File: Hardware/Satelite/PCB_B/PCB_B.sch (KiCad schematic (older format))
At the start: 31 parts, among them IC1 MCP1642B-50I_MS, J1 Conector_PCB_B-C, J2 Conector_PCB_A-B, M1 Spacer, M2 Spacer, M3 Spacer, U1 MIC5323-3.3YD5_TR

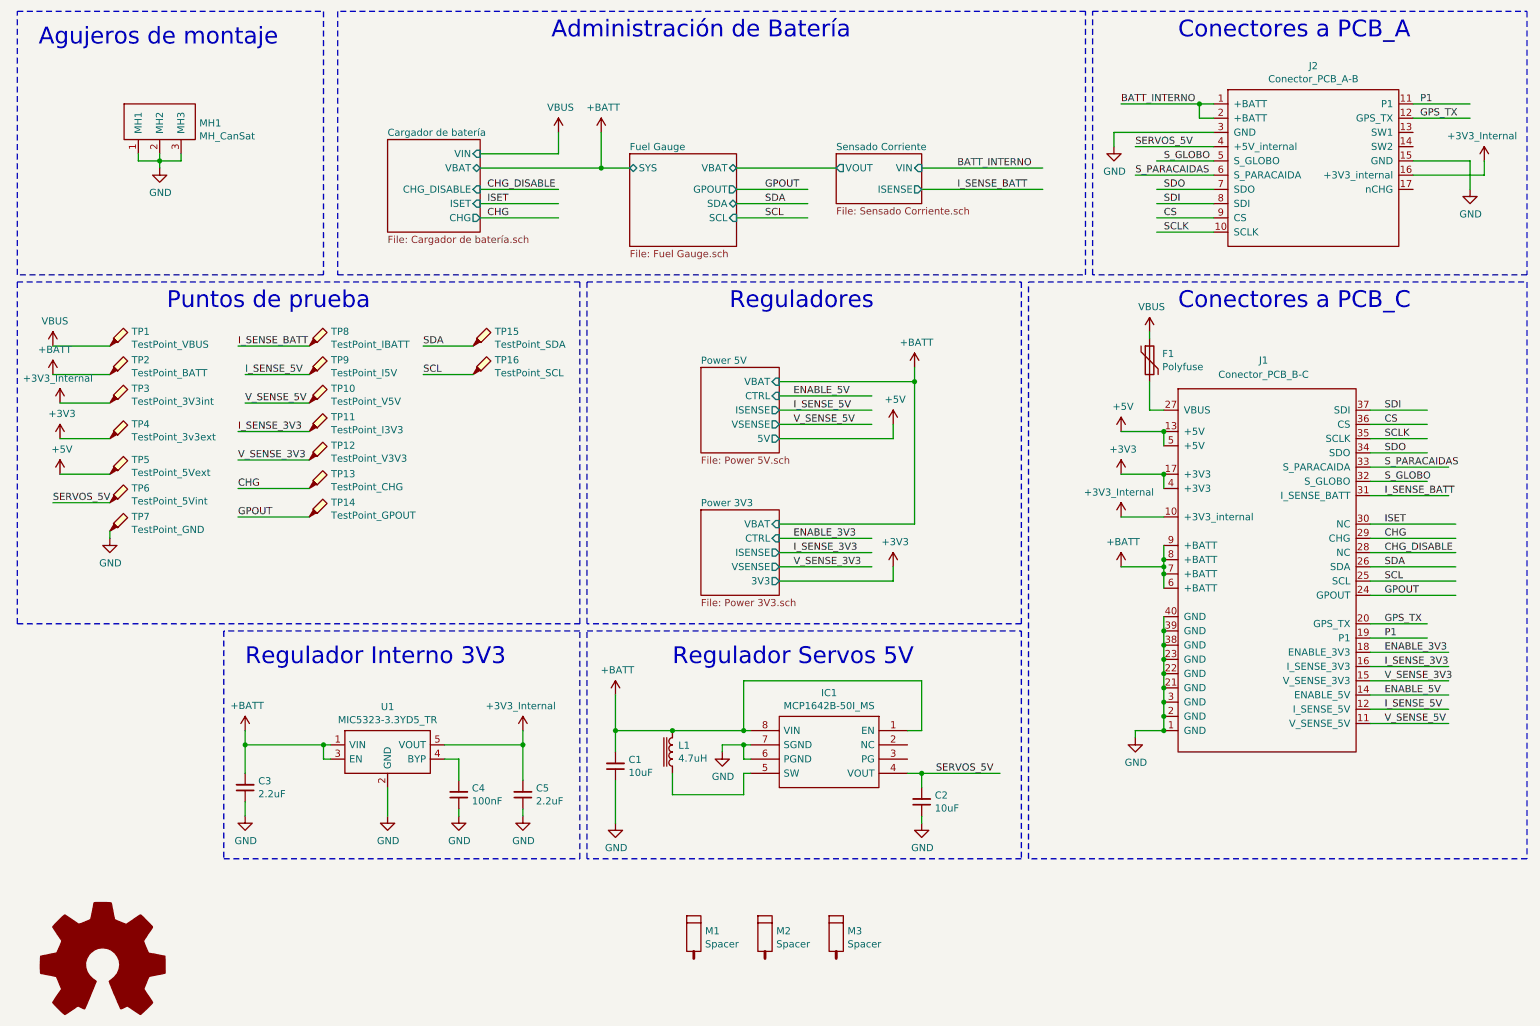
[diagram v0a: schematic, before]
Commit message: Arreglos en PCB_A y PCB_B:
- El CI cargador de batería ya no alimenta al sistema, al conectar un cargador el mismo alimenta a la batería y al sistema de manera simultánea
- Ya no es necesario encender el CanSat para cargar la batería
- El interruptor del PCB_A ahora apaga todo el sistema independientemente si se está cargando o no la batería
- Agregado LED indicador de carga de batería
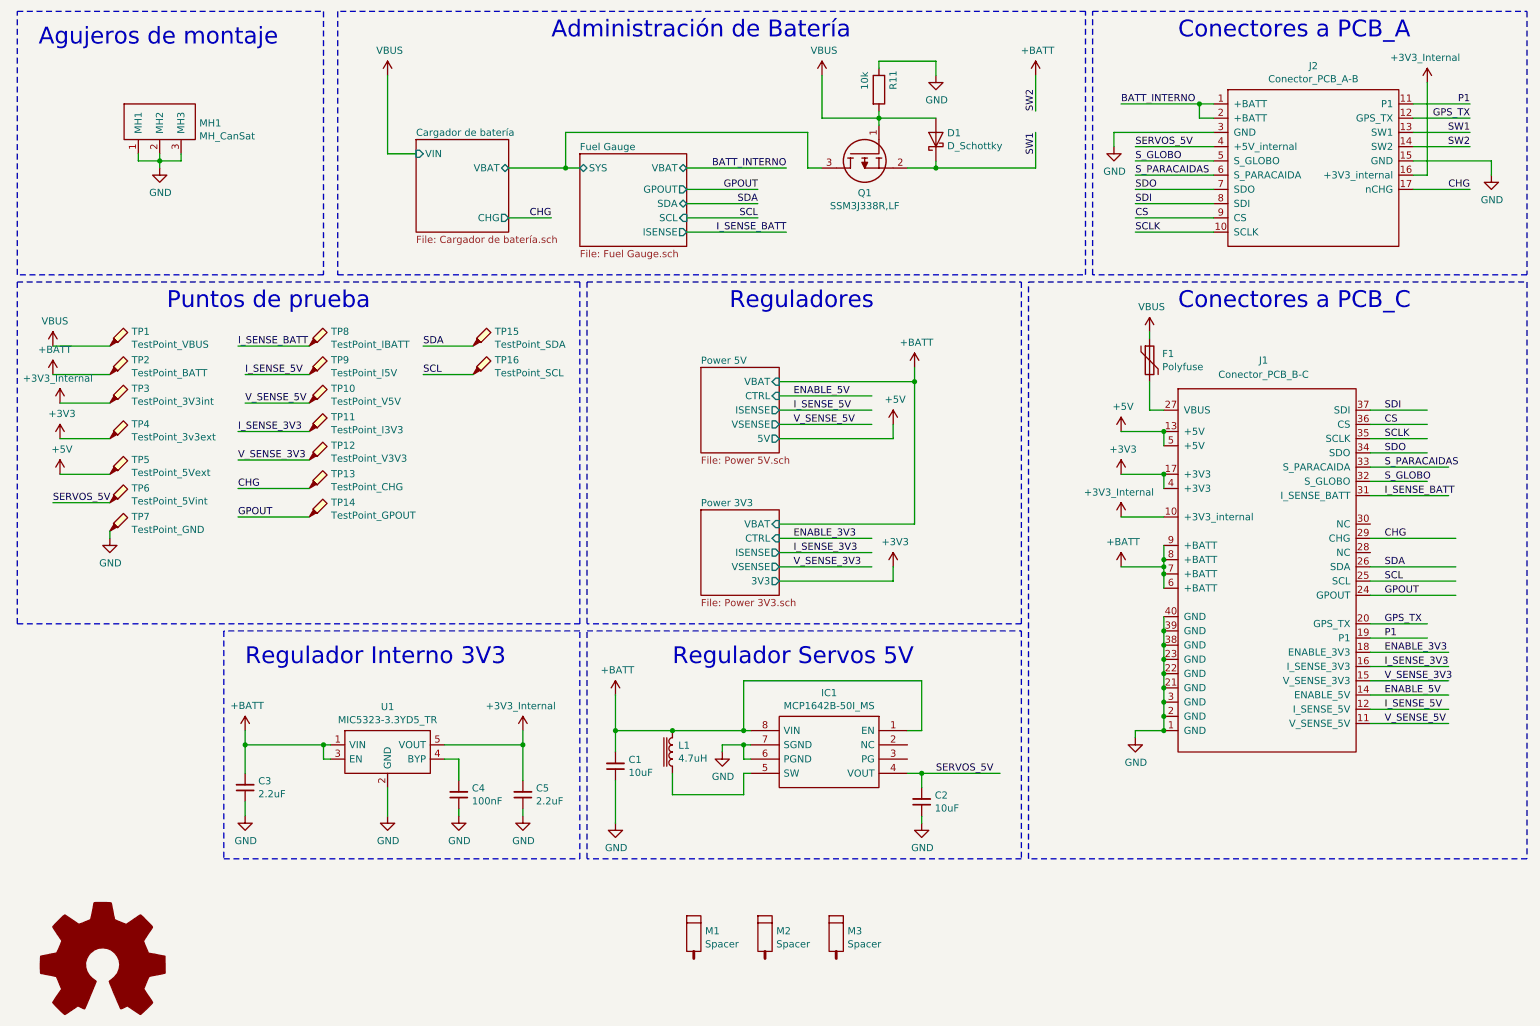
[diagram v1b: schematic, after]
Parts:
- added D1: D_Schottky, Diode_SMD:D_SMB, symbol Device:D_Schottky
- added Q1: SSM3J338R,LF, SamacSys_Parts:SSM3J332RLFT, symbol SamacSys_Parts:SSM3J338R,LF
- added R11: 10k, Capacitor_SMD:C_0603_1608Metric_Pad1.05x0.95mm_HandSolder, symbol Device:R
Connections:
- net labels added: SW1, SW2
- net labels removed: CHG_DISABLE, ISET
- wire segments 151 -> 165

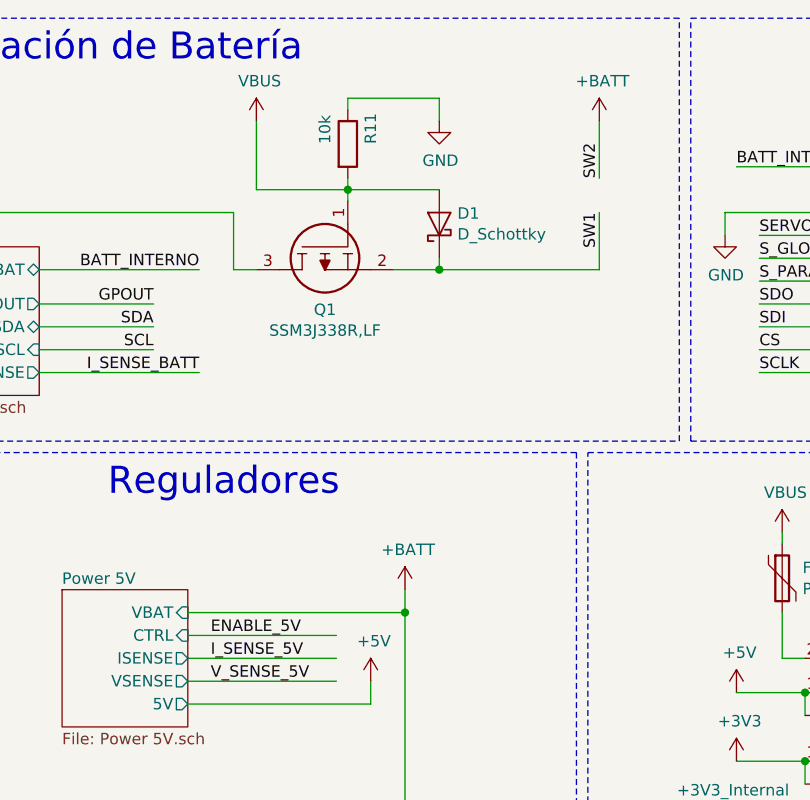
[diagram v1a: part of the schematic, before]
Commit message: Corregido MOSFET Q1 con drenador y surtidor invertidos
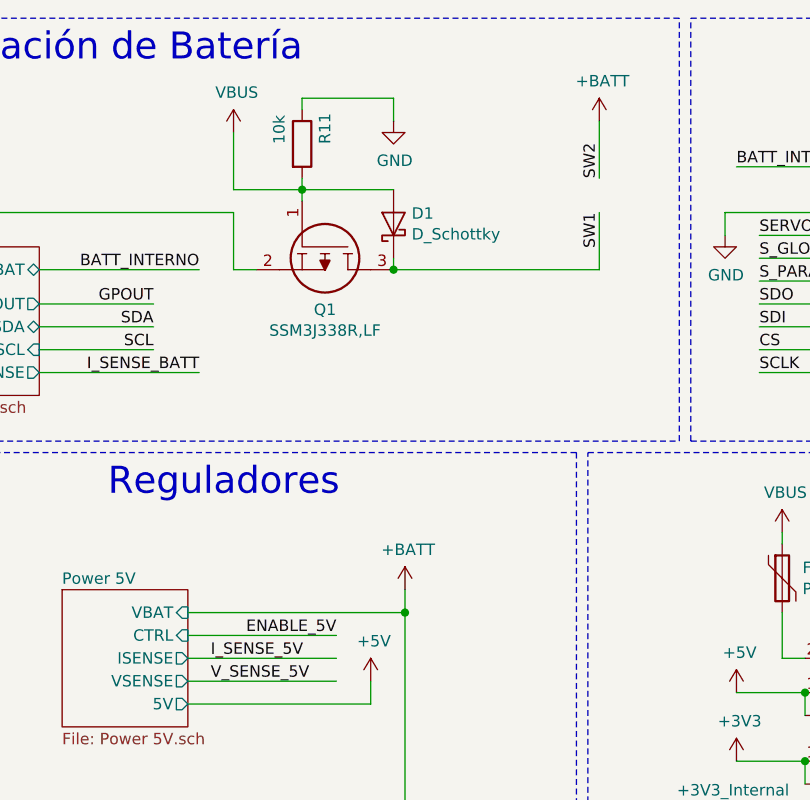
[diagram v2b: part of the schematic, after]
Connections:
- wire segments 165 -> 164
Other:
- moved on the sheet: D1, R11
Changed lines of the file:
@@
 Text Label 6000 4250 0    50   ~ 0
 ENABLE_3V3
-Text Label 6000 3250 0    50   ~ 0
+Text Label 6550 3250 2    50   ~ 0
 ENABLE_5V
 Wire Wire Line
@@
 Text Label 5950 1650 2    50   ~ 0
 BATT_INTERNO
-Connection ~ 7000 1650
-Wire Wire Line
-	7000 1650 7700 1650
-Wire Wire Line
-	6800 1650 7000 1650
-Wire Wire Line
-	7000 1600 7000 1650
 $Comp
 L Device:D_Schottky D1
 U 1 1 5CD2E872
-P 7000 1450
-F 0 "D1" V 7046 1371 50  0000 R CNN
-F 1 "D_Schottky" V 6955 1371 50  0000 R CNN
-F 2 "Diode_SMD:D_SMB" H 7000 1450 50  0001 C CNN
-F 3 "~" H 7000 1450 50  0001 C CNN
-F 4 "MBRS2040LT3G" V 7000 1450 50  0001 C CNN "Manufacturer Part Number"
-	1    7000 1450
+P 6800 1450
+F 0 "D1" V 6846 1371 50  0000 R CNN
+F 1 "D_Schottky" V 6755 1371 50  0000 R CNN
+F 2 "Diode_SMD:D_SMB" H 6800 1450 50  0001 C CNN
+F 3 "~" H 6800 1450 50  0001 C CNN
+F 4 "MBRS2040LT3G" V 6800 1450 50  0001 C CNN "Manufacturer Part Number"
+	1    6800 1450
 	0    -1   -1   0
 $EndComp
 Wire Wire Line
-	6600 1250 6600 1300
-Wire Wire Line
-	7000 900  7000 1000
-Wire Wire Line
-	6600 950  6600 900
-Connection ~ 6600 1300
-Wire Wire Line
-	6600 1350 6600 1300
-Wire Wire Line
-	7000 1300 6600 1300
+	6400 1250 6400 1300
+Wire Wire Line
+	6800 900  6800 1000
+Wire Wire Line
+	6400 950  6400 900
+Connection ~ 6400 1300
+Wire Wire Line
+	6400 1350 6400 1300
+Wire Wire Line
+	6800 1300 6400 1300
 $Comp
 L power:GND #PWR?
 U 1 1 5CCDA8EC
-P 7000 1000
+P 6800 1000
 AR Path="/5BB6C3A1/5CCDA8EC" Ref="#PWR?"  Part="1"
 AR Path="/5BB6C83B/5CCDA8EC" Ref="#PWR?"  Part="1"
 AR Path="/5BC14C3C/5CCDA8EC" Ref="#PWR?"  Part="1"
 AR Path="/5CCDA8EC" Ref="#PWR017"  Part="1"
-F 0 "#PWR017" H 7000 750 50  0001 C CNN
-F 1 "GND" H 7005 827 50  0000 C CNN
-F 2 "" H 7000 1000 50  0001 C CNN
-F 3 "" H 7000 1000 50  0001 C CNN
-	1    7000 1000
+F 0 "#PWR017" H 6800 750 50  0001 C CNN
+F 1 "GND" H 6805 827 50  0000 C CNN
+F 2 "" H 6800 1000 50  0001 C CNN
+F 3 "" H 6800 1000 50  0001 C CNN
+	1    6800 1000
 	1    0    0    -1
 $EndComp
@@
 L Device:R R?
 U 1 1 5CCCB39F
-P 6600 1100
+P 6400 1100
 AR Path="/5BA17F9C/5CCCB39F" Ref="R?"  Part="1"
 AR Path="/5BA1A7F9/5CCCB39F" Ref="R?"  Part="1"
@@
 AR Path="/5BB1631B/5CCCB39F" Ref="R?"  Part="1"
 AR Path="/5BC28DAC/5CCCB39F" Ref="R?"  Part="1"
-F 0 "R11" V 6700 1100 50  0000 L CNN
-F 1 "10k" V 6500 1100 50  0000 L CNN
-F 2 "Capacitor_SMD:C_0603_1608Metric_Pad1.05x0.95mm_HandSolder" V 6530 1100 50  0001 C CNN
-F 3 "~" H 6600 1100 50  0001 C CNN
-F 4 "RC0603JR-0710KL" V 6600 1100 50  0001 C CNN "Manufacturer Part Number"
-	1    6600 1100
+F 0 "R11" V 6500 1100 50  0000 L CNN
+F 1 "10k" V 6300 1100 50  0000 L CNN
+F 2 "Capacitor_SMD:C_0603_1608Metric_Pad1.05x0.95mm_HandSolder" V 6330 1100 50  0001 C CNN
+F 3 "~" H 6400 1100 50  0001 C CNN
+F 4 "RC0603JR-0710KL" V 6400 1100 50  0001 C CNN "Manufacturer Part Number"
+	1    6400 1100
 	1    0    0    -1
 $EndComp
@@
 L SamacSys_Parts:SSM3J338R,LF Q1
 U 1 1 5CCA0FA0
-P 6600 1350
-F 0 "Q1" V 7075 1450 50  0000 C CNN
-F 1 "SSM3J338R,LF" V 7166 1450 50  0000 C CNN
-F 2 "SamacSys_Parts:SSM3J332RLFT" H 7050 1300 50  0001 L CNN
-F 3 "http://toshiba.semicon-storage.com/info/docget.jsp?did=30384&prodName=SSM3J338R" H 7050 1200 50  0001 L CNN
-F 4 "MOSFET Small-signal MOSFET Vdss= -12V, ID= -6A" H 7050 1100 50  0001 L CNN "Description"
-F 5 "Toshiba" H 7050 900 50  0001 L CNN "Manufacturer_Name"
-F 6 "SSM3J338R,LF" H 7050 800 50  0001 L CNN "Manufacturer Part Number"
-F 7 "SSM3J338R,LF" H 7050 500 50  0001 L CNN "Arrow Part Number"
-F 8 "https://www.arrow.com/en/products/ssm3j338rlf/toshiba" H 7050 400 50  0001 L CNN "Arrow Price/Stock"
-	1    6600 1350
-	0    -1   1    0
+P 6400 1350
+F 0 "Q1" V 6875 1450 50  0000 C CNN
+F 1 "SSM3J338R,LF" V 6966 1450 50  0000 C CNN
+F 2 "SamacSys_Parts:SSM3J332RLFT" H 6850 1300 50  0001 L CNN
+F 3 "http://toshiba.semicon-storage.com/info/docget.jsp?did=30384&prodName=SSM3J338R" H 6850 1200 50  0001 L CNN
+F 4 "MOSFET Small-signal MOSFET Vdss= -12V, ID= -6A" H 6850 1100 50  0001 L CNN "Description"
+F 5 "Toshiba" H 6850 900 50  0001 L CNN "Manufacturer_Name"
+F 6 "SSM3J338R,LF" H 6850 800 50  0001 L CNN "Manufacturer Part Number"
+F 7 "SSM3J338R,LF" H 6850 500 50  0001 L CNN "Arrow Part Number"
+F 8 "https://www.arrow.com/en/products/ssm3j338rlf/toshiba" H 6850 400 50  0001 L CNN "Arrow Price/Stock"
+	1    6400 1350
+	0    1    1    0
 $EndComp
 $Sheet
@@
 	4000 1650 4400 1650
 Wire Wire Line
-	6600 1300 6200 1300
+	6400 1300 6100 1300
 $Comp
 L power:VBUS #PWR0111
@@
 $EndComp
 Wire Wire Line
-	6600 900  7000 900
+	6400 900  6800 900
 Wire Wire Line
 	3150 1000 3150 1550
@@
 L power:VBUS #PWR08
 U 1 1 5CE2ECED
-P 6200 1000
-F 0 "#PWR08" H 6200 850 50  0001 C CNN
-F 1 "VBUS" H 6214 1175 50  0000 C CNN
-F 2 "" H 6200 1000 50  0001 C CNN
-F 3 "" H 6200 1000 50  0001 C CNN
-	1    6200 1000
-	1    0    0    -1
-$EndComp
-Wire Wire Line
-	6200 1300 6200 1000
+P 6100 1050
+F 0 "#PWR08" H 6100 900 50  0001 C CNN
+F 1 "VBUS" H 6114 1225 50  0000 C CNN
+F 2 "" H 6100 1050 50  0001 C CNN
+F 3 "" H 6100 1050 50  0001 C CNN
+	1    6100 1050
+	1    0    0    -1
+$EndComp
+Wire Wire Line
+	6100 1300 6100 1050
 Wire Wire Line
 	5950 2100 5250 2100
@@
 Wire Wire Line
 	10750 1800 10350 1800
+Wire Wire Line
+	6800 1650 7700 1650
+Wire Wire Line
+	6800 1600 6800 1650
+Connection ~ 6800 1650
 $EndSCHEMATC

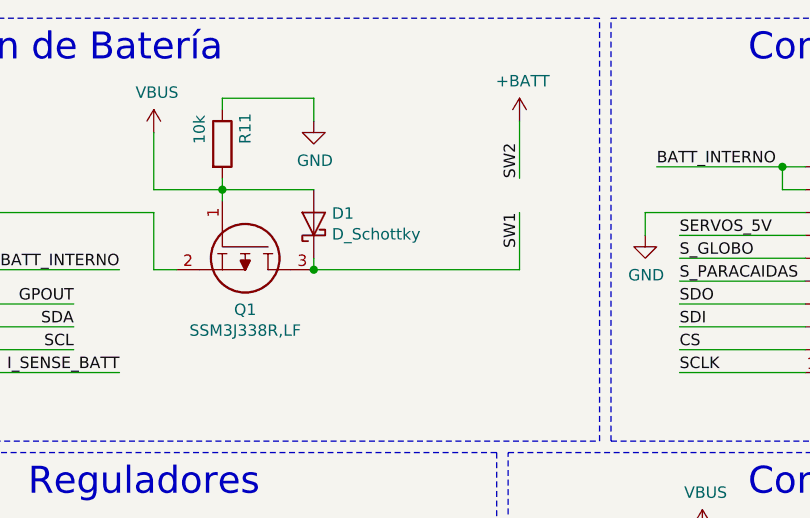
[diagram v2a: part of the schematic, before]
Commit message: Nuevo conector entre PCB_B y PCB_C, más fácil de soldar y robusto
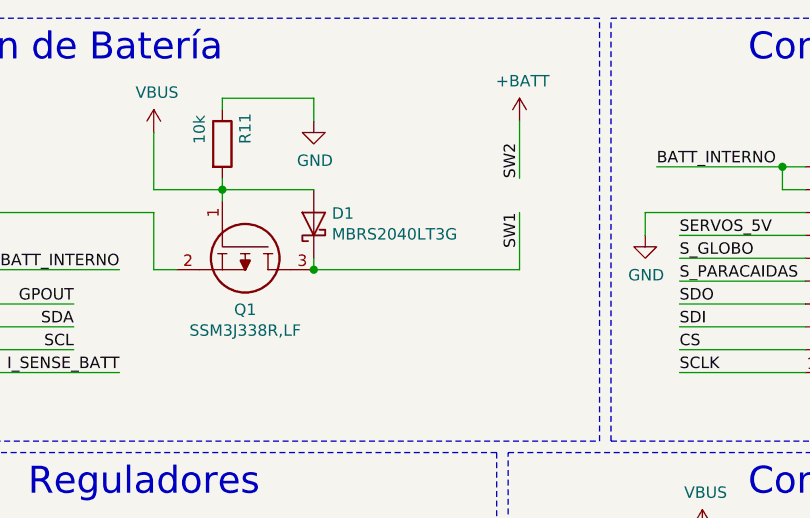
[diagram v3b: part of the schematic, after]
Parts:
- D1: value D_Schottky -> MBRS2040LT3G
- J1: Manufacturer Part Number 10132798-022100LF -> 52465-2071
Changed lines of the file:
@@
 F 2 "AXTEC:Conector_PCB_B-C_Lado_B" H 9200 4650 50  0001 C CNN
 F 3 "" H 9200 4650 50  0001 C CNN
-F 4 "10132798-022100LF" H 9300 3900 50  0001 C CNN "Manufacturer Part Number"
+F 4 "52465-2071" H 9300 3900 50  0001 C CNN "Manufacturer Part Number"
 F 5 "2" H 9300 3900 50  0001 C CNN "Quantity"
 	1    9300 3900
@@
 P 6800 1450
 F 0 "D1" V 6846 1371 50  0000 R CNN
-F 1 "D_Schottky" V 6755 1371 50  0000 R CNN
+F 1 "MBRS2040LT3G" V 6755 1371 50  0000 R CNN
 F 2 "Diode_SMD:D_SMB" H 6800 1450 50  0001 C CNN
 F 3 "~" H 6800 1450 50  0001 C CNN
